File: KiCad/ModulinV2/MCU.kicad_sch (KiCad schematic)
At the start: 15 parts, among them IC1 STM32F401VET6, SW1 SW_Push, SW2 SW_Push

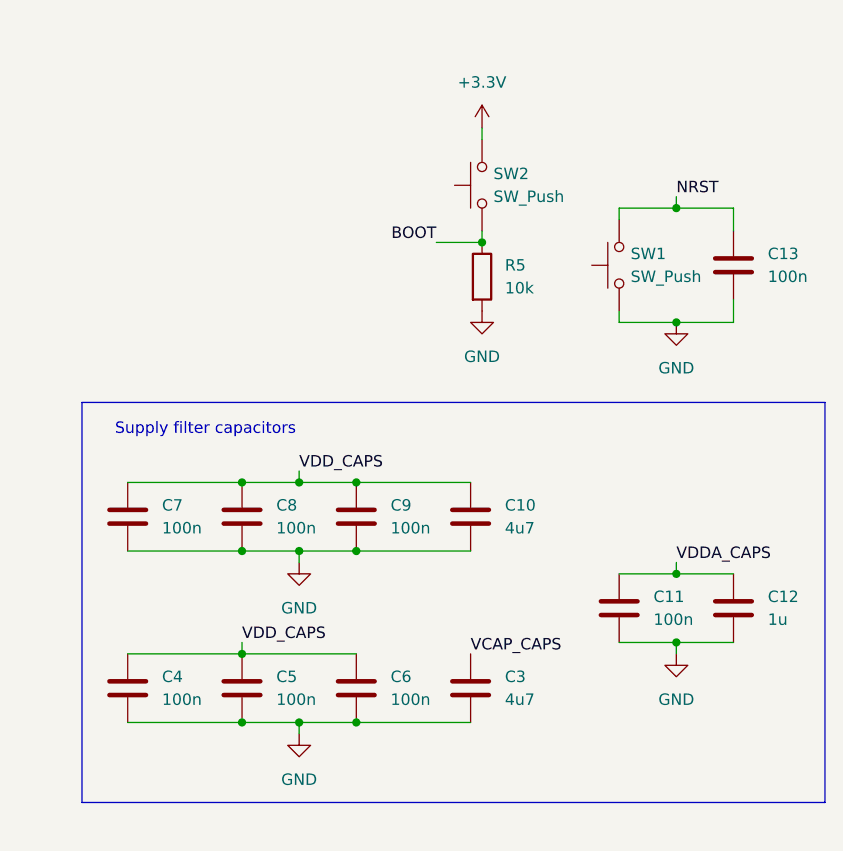
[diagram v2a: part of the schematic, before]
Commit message: Added initial schematic of VCO and repaired some schematic issues
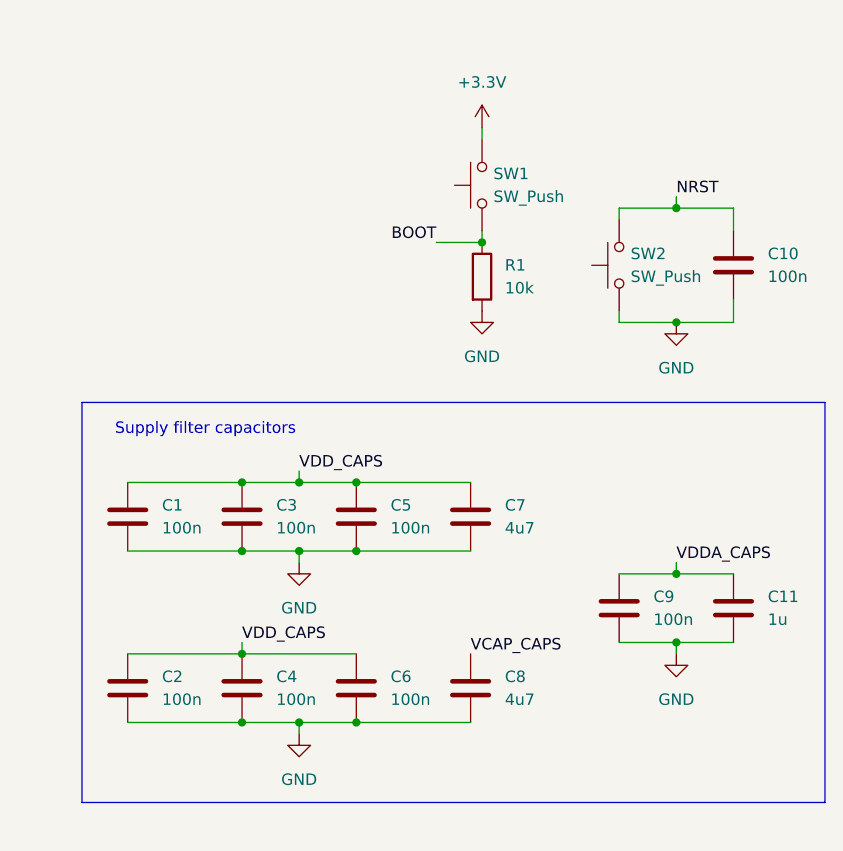
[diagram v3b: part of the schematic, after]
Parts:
- renumbered C7 to C1, C13 to C10, C12 to C11, C4 to C2, C8 to C3, C5 to C4, C9 to C5, C10 to C7, C3 to C8, C11 to C9, R5 to R1, SW2 to SW1, SW1 to SW2
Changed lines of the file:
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@@
 		(dnp no)
 		(fields_autoplaced yes)
-		(property "Reference" "C11"
+		(property "Reference" "C9"
 			(at 264.16 140.9699 0)
 			(effects
@@
 			(project "ModulinV2"
 				(path "/c6b34a57-3941-4b56-8b80-1848c7f41082/2f38494c-2f9d-4537-8bdc-28b3add05107"
-					(reference "C11")
+					(reference "C9")
 					(unit 1)
 				)
@@
 		(dnp no)
 		(fields_autoplaced yes)
-		(property "Reference" "#PWR022"
+		(property "Reference" "#PWR06"
 			(at 245.11 92.71 0)
 			(effects
@@
 			(project ""
 				(path "/c6b34a57-3941-4b56-8b80-1848c7f41082/2f38494c-2f9d-4537-8bdc-28b3add05107"
-					(reference "#PWR022")
+					(reference "#PWR06")
 					(unit 1)
 				)
@@
 		(dnp no)
 		(fields_autoplaced yes)
-		(property "Reference" "C10"
+		(property "Reference" "C7"
 			(at 247.65 130.8099 0)
 			(effects
@@
 			(project "ModulinV2"
 				(path "/c6b34a57-3941-4b56-8b80-1848c7f41082/2f38494c-2f9d-4537-8bdc-28b3add05107"
-					(reference "C10")
+					(reference "C7")
 					(unit 1)
 				)
@@
 		(dnp no)
 		(fields_autoplaced yes)
-		(property "Reference" "#PWR018"
+		(property "Reference" "#PWR09"
 			(at 266.7 153.67 0)
 			(effects
@@
 			(project "ModulinV2"
 				(path "/c6b34a57-3941-4b56-8b80-1848c7f41082/2f38494c-2f9d-4537-8bdc-28b3add05107"
-					(reference "#PWR018")
+					(reference "#PWR09")
 					(unit 1)
 				)
@@
 		(dnp no)
 		(fields_autoplaced yes)
-		(property "Reference" "#PWR020"
+		(property "Reference" "#PWR08"
 			(at 266.7 116.84 0)
 			(effects
@@
 			(project "ModulinV2"
 				(path "/c6b34a57-3941-4b56-8b80-1848c7f41082/2f38494c-2f9d-4537-8bdc-28b3add05107"
-					(reference "#PWR020")
+					(reference "#PWR08")
 					(unit 1)
 				)
@@
 		(dnp no)
 		(fields_autoplaced yes)
-		(property "Reference" "#PWR017"
+		(property "Reference" "#PWR04"
 			(at 224.79 143.51 0)
 			(effects
@@
 			(project ""
 				(path "/c6b34a57-3941-4b56-8b80-1848c7f41082/2f38494c-2f9d-4537-8bdc-28b3add05107"
-					(reference "#PWR017")
+					(reference "#PWR04")
 					(unit 1)
 				)
@@
 		(dnp no)
 		(fields_autoplaced yes)
-		(property "Reference" "#PWR019"
+		(property "Reference" "#PWR05"
 			(at 224.79 162.56 0)
 			(effects
@@
 			(project "ModulinV2"
 				(path "/c6b34a57-3941-4b56-8b80-1848c7f41082/2f38494c-2f9d-4537-8bdc-28b3add05107"
-					(reference "#PWR019")
+					(reference "#PWR05")
 					(unit 1)
 				)
@@
 		(dnp no)
 		(fields_autoplaced yes)
-		(property "Reference" "C13"
+		(property "Reference" "C10"
 			(at 276.86 102.8699 0)
 			(effects
@@
 			(project "ModulinV2"
 				(path "/c6b34a57-3941-4b56-8b80-1848c7f41082/2f38494c-2f9d-4537-8bdc-28b3add05107"
-					(reference "C13")
+					(reference "C10")
 					(unit 1)
 				)
@@
 		(dnp no)
 		(fields_autoplaced yes)
-		(property "Reference" "C12"
+		(property "Reference" "C11"
 			(at 276.86 140.9699 0)
 			(effects
@@
 			(project "ModulinV2"
 				(path "/c6b34a57-3941-4b56-8b80-1848c7f41082/2f38494c-2f9d-4537-8bdc-28b3add05107"
-					(reference "C12")
+					(reference "C11")
 					(unit 1)
 				)
@@
 		(dnp no)
 		(fields_autoplaced yes)
-		(property "Reference" "#PWR01"
+		(property "Reference" "#PWR02"
 			(at 83.82 39.37 0)
 			(effects
@@
 			(project ""
 				(path "/c6b34a57-3941-4b56-8b80-1848c7f41082/2f38494c-2f9d-4537-8bdc-28b3add05107"
-					(reference "#PWR01")
+					(reference "#PWR02")
 					(unit 1)
 				)
@@
 		(dnp no)
 		(fields_autoplaced yes)
-		(property "Reference" "R5"
+		(property "Reference" "R1"
 			(at 247.65 104.1399 0)
 			(effects
@@
 			(project ""
 				(path "/c6b34a57-3941-4b56-8b80-1848c7f41082/2f38494c-2f9d-4537-8bdc-28b3add05107"
-					(reference "R5")
+					(reference "R1")
 					(unit 1)
 				)
@@
 		(dnp no)
 		(fields_autoplaced yes)
-		(property "Reference" "SW1"
+		(property "Reference" "SW2"
 			(at 261.62 102.8699 90)
 			(effects
@@
 			(project ""
 				(path "/c6b34a57-3941-4b56-8b80-1848c7f41082/2f38494c-2f9d-4537-8bdc-28b3add05107"
-					(reference "SW1")
+					(reference "SW2")
 					(unit 1)
 				)
@@
 		(dnp no)
 		(fields_autoplaced yes)
-		(property "Reference" "C9"
+		(property "Reference" "C5"
 			(at 234.95 130.8099 0)
 			(effects
@@
 			(project "ModulinV2"
 				(path "/c6b34a57-3941-4b56-8b80-1848c7f41082/2f38494c-2f9d-4537-8bdc-28b3add05107"
-					(reference "C9")
+					(reference "C5")
 					(unit 1)
 				)
@@
 		(dnp no)
 		(fields_autoplaced yes)
-		(property "Reference" "C8"
+		(property "Reference" "C3"
 			(at 222.25 130.8099 0)
 			(effects
@@
 			(project "ModulinV2"
 				(path "/c6b34a57-3941-4b56-8b80-1848c7f41082/2f38494c-2f9d-4537-8bdc-28b3add05107"
-					(reference "C8")
+					(reference "C3")
 					(unit 1)
 				)
@@
 		(dnp no)
 		(fields_autoplaced yes)
-		(property "Reference" "SW2"
+		(property "Reference" "SW1"
 			(at 246.38 93.9799 90)
 			(effects
@@
 			(project "ModulinV2"
 				(path "/c6b34a57-3941-4b56-8b80-1848c7f41082/2f38494c-2f9d-4537-8bdc-28b3add05107"
-					(reference "SW2")
+					(reference "SW1")
 					(unit 1)
 				)
@@
 		(dnp no)
 		(fields_autoplaced yes)
-		(property "Reference" "C3"
+		(property "Reference" "C8"
 			(at 247.65 149.8599 0)
 			(effects
@@
 			(project ""
 				(path "/c6b34a57-3941-4b56-8b80-1848c7f41082/2f38494c-2f9d-4537-8bdc-28b3add05107"
-					(reference "C3")
+					(reference "C8")
 					(unit 1)
 				)
@@
 		(dnp no)
 		(fields_autoplaced yes)
-		(property "Reference" "#PWR016"
+		(property "Reference" "#PWR01"
 			(at 68.58 39.37 0)
 			(effects
@@
 			(project ""
 				(path "/c6b34a57-3941-4b56-8b80-1848c7f41082/2f38494c-2f9d-4537-8bdc-28b3add05107"
-					(reference "#PWR016")
+					(reference "#PWR01")
 					(unit 1)
 				)
@@
 		(dnp no)
 		(fields_autoplaced yes)
-		(property "Reference" "C5"
+		(property "Reference" "C4"
 			(at 222.25 149.8599 0)
 			(effects
@@
 			(project "ModulinV2"
 				(path "/c6b34a57-3941-4b56-8b80-1848c7f41082/2f38494c-2f9d-4537-8bdc-28b3add05107"
-					(reference "C5")
+					(reference "C4")
 					(unit 1)
 				)
@@
 		(dnp no)
 		(fields_autoplaced yes)
-		(property "Reference" "C7"
+		(property "Reference" "C1"
 			(at 209.55 130.8099 0)
 			(effects
@@
 			(project "ModulinV2"
 				(path "/c6b34a57-3941-4b56-8b80-1848c7f41082/2f38494c-2f9d-4537-8bdc-28b3add05107"
-					(reference "C7")
+					(reference "C1")
 					(unit 1)
 				)
@@
 		(dnp no)
 		(fields_autoplaced yes)
-		(property "Reference" "#PWR021"
+		(property "Reference" "#PWR07"
 			(at 245.11 115.57 0)
 			(effects
@@
 			(project "ModulinV2"
 				(path "/c6b34a57-3941-4b56-8b80-1848c7f41082/2f38494c-2f9d-4537-8bdc-28b3add05107"
-					(reference "#PWR021")
+					(reference "#PWR07")
 					(unit 1)
 				)
@@
 		(on_board yes)
 		(dnp no)
-		(property "Reference" "C4"
+		(property "Reference" "C2"
 			(at 209.55 149.8599 0)
 			(effects
@@
 			(project "ModulinV2"
 				(path "/c6b34a57-3941-4b56-8b80-1848c7f41082/2f38494c-2f9d-4537-8bdc-28b3add05107"
-					(reference "C4")
-					(unit 1)
-				)
+					(reference "C2")
+					(unit 1)
+				)

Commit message: Finished 1.0 of the VCO and started making the waveform select module
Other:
- company: Rasmus Palk -> (none)
- title: (none) -> Microcontroller
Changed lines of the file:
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@@
 	(paper "A4")
 	(title_block
-		(company "Rasmus Palk")
+		(title "Microcontroller")
+		(date "2025-07-13")
+		(rev "1.0")
+		(comment 1 "Instructor: Kaiser Pärnamets")
+		(comment 2 "By: Rasmus Palk")
 	)
 	(rectangle

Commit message: Modified USB connection and added LEDs
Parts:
- added C1, C13: 2u2, symbol Device:C
- added D5: CDBU0530, DIOM179X85N, symbol CDBU0530:CDBU0530
- added IC2: STM32F401RET6, symbol STM32F401RET6:STM32F401RET6_Alt
- added J1: USB4105-GF-A, symbol USB4105-GF-A:USB4105-GF-A
- added JP3, JP4: ADSR+LFO, symbol Jumper:SolderJumper_2_Open
- added LED1: 150212M173123, 150212M173123, symbol 150212M173123:150212M173123
- added LED2: 150060VS75000, LEDC1608X80N, symbol 150060VS75000:150060VS75000
- added Q3, Q4, Q5: BC847B,215, BC847B215, symbol BC847B_215:BC847B,215
- added R87, R88: 5k1, symbol Device:R
- added R89, R91: 51, symbol Device:R
- added R90: 130, symbol Device:R
- added R92, R93, R94: 68k, symbol Device:R
- added R95: 300, symbol Device:R
- C10: renamed from C7; value 4u7 -> 2u2
- C2: renamed from C8; value 4u7 -> 2u2
- renumbered C10 to C11, C2 to C12, C9 to C3, C11 to C4, C1 to C5, C4 to C6, C3 to C7, C6 to C8, C5 to C9
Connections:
- net +3.3V: now also C13.1, IC2.1 (VBAT), IC2.13 (VDDA/VREF+), IC2.19 (VDD_1), IC2.32 (VDD_2), IC2.48 (VDD_3), IC2.64 (VDD_4), LED1.1
- net BOOT: now also IC2.60 (BOOT0)
- net GND: now also C1.2, C13.2, IC2.12 (VSSA/VREF-), IC2.18 (VSS_1), IC2.31 (VSS_2), IC2.47 (VSS_3), IC2.63 (VSS_4), J1.A1 (GND), J1.A12 (GND), J1.B1 (GND), J1.B12 (GND), J1.S1 (SHIELD), LED2.1 (K), Q3.2 (E), Q4.2 (E), Q5.2 (E), R87.2, R88.2
- net NRST: now also IC2.7 (NRST)
- net ADSR_SPI_CLK renamed ADSR_CLK
- net ADSR_CLK: now also IC2.51 (PC10), JP4.1 (A)
- net ADSR_SPI_CS1 renamed ADSR_CS1
- net ADSR_CS1: now also IC2.54 (PD2)
- net ADSR_SPI_CS2 renamed ADSR_CS2
- net ADSR_CS2: now also IC2.50 (PA15)
- net ADSR_SPI_MOSI renamed ADSR_MOSI
- net ADSR_MOSI: now also IC2.53 (PC12), JP3.1 (A)
- net LFO_SPI_CLK renamed LFO_CLK
- net LFO_CLK: now also JP4.2 (B)
- net LFO_SPI_CS renamed LFO_CS
- net LFO_CS: now also IC2.40 (PC9)
- net LFO_SPI_MISO renamed LFO_MISO
- net LFO_MISO: now also IC2.52 (PC11)
- net LFO_SPI_MOSI renamed LFO_MOSI
- net LFO_MOSI: now also JP3.2 (B)
- net RIBBON_ADC_SPI_CLK renamed ADC_CLK
- net ADC_CLK: now also IC2.21 (PA5)
- net RIBBON_ADC_SPI_CS1 renamed ADC_CS1
- net ADC_CS1: now also IC2.20 (PA4)
- net RIBBON_ADC_SPI_CS2 renamed ADC_CS2
- net ADC_CS2: now also IC2.23 (PA7)
- net RIBBON_ADC_SPI_MISO renamed ADC_MISO
- net ADC_MISO: now also IC2.22 (PA6)
- net RIBBON_DAC_SPI_CLK renamed INT_DAC_CLK
- net INT_DAC_CLK: now also IC2.34 (PB13)
- net RIBBON_DAC_SPI_CS1 renamed INT_DAC_CS1
- net INT_DAC_CS1: now also IC2.33 (PB12)
- net RIBBON_DAC_SPI_CS2 renamed INT_DAC_CS2
- net INT_DAC_CS2: now also IC2.35 (PB14)
- net RIBBON_DAC_SPI_MOSI renamed INT_DAC_MOSI
- net INT_DAC_MOSI: now also IC2.36 (PB15)
- net VCAP_CAPS renamed VCAP
- net VCAP: now also C1.1, IC2.30 (VCAP1)
- new net: D5.2 (A), J1.A4 (VBUS), J1.A9 (VBUS), J1.B4 (VBUS), J1.B9 (VBUS), R95.1
- new net: LED2.2 (A), R95.2
- new net: Q3.3 (C), R89.1
- new net: LED1.2, R89.2
- new net: Q5.1 (B), R93.1
- new net: LED1.3, R91.1
- new net: LED1.4, R90.1
- new net: Q5.3 (C), R91.2
- new net: Q4.1 (B), R92.1
- new net: J1.A5 (CC1), R88.1
- new net: J1.B5 (CC2), R87.1
- new net: Q4.3 (C), R90.2
- new net: Q3.1 (B), R94.1
- new net +5V: D5.1 (K)
- new net ADSR_ENC_A: IC2.14 (PA0)
- new net ADSR_ENC_B: IC2.15 (PA1)
- new net LED_B: IC2.29 (PB10), R94.2
- new net LED_G: IC2.62 (PB9), R93.2
- new net LED_R: IC2.61 (PB8), R92.2
- new net LFO_ENC_A: IC2.41 (PA8)
- new net LFO_ENC_B: IC2.42 (PA9)
- new net SCL: IC2.58 (PB6)
- new net SDA: IC2.59 (PB7)
- new net SWCLK: IC2.49 (PA14)
- new net SWDIO: IC2.46 (PA13)
- new net SWO: IC2.55 (PB3)
- new net USB_DM: IC2.44 (PA11), J1.A7 (D-), J1.B7 (D-)
- new net USB_DP: IC2.45 (PA12), J1.A6 (D+), J1.B6 (D+)
- no-connect marks 0 -> 2
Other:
- note added: "ADSR & LFO SPI connecting"
- note added: "Reset and Boot buttons"
- note added: "VCAP"
- note added: "VDD"
- note added: "VDDA & VREF"
- note removed: "Supply filter capacitors"
- moved on the sheet: C10, C11, C12, C2, C3, C4, C5, C6, C7, C8, C9, IC1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

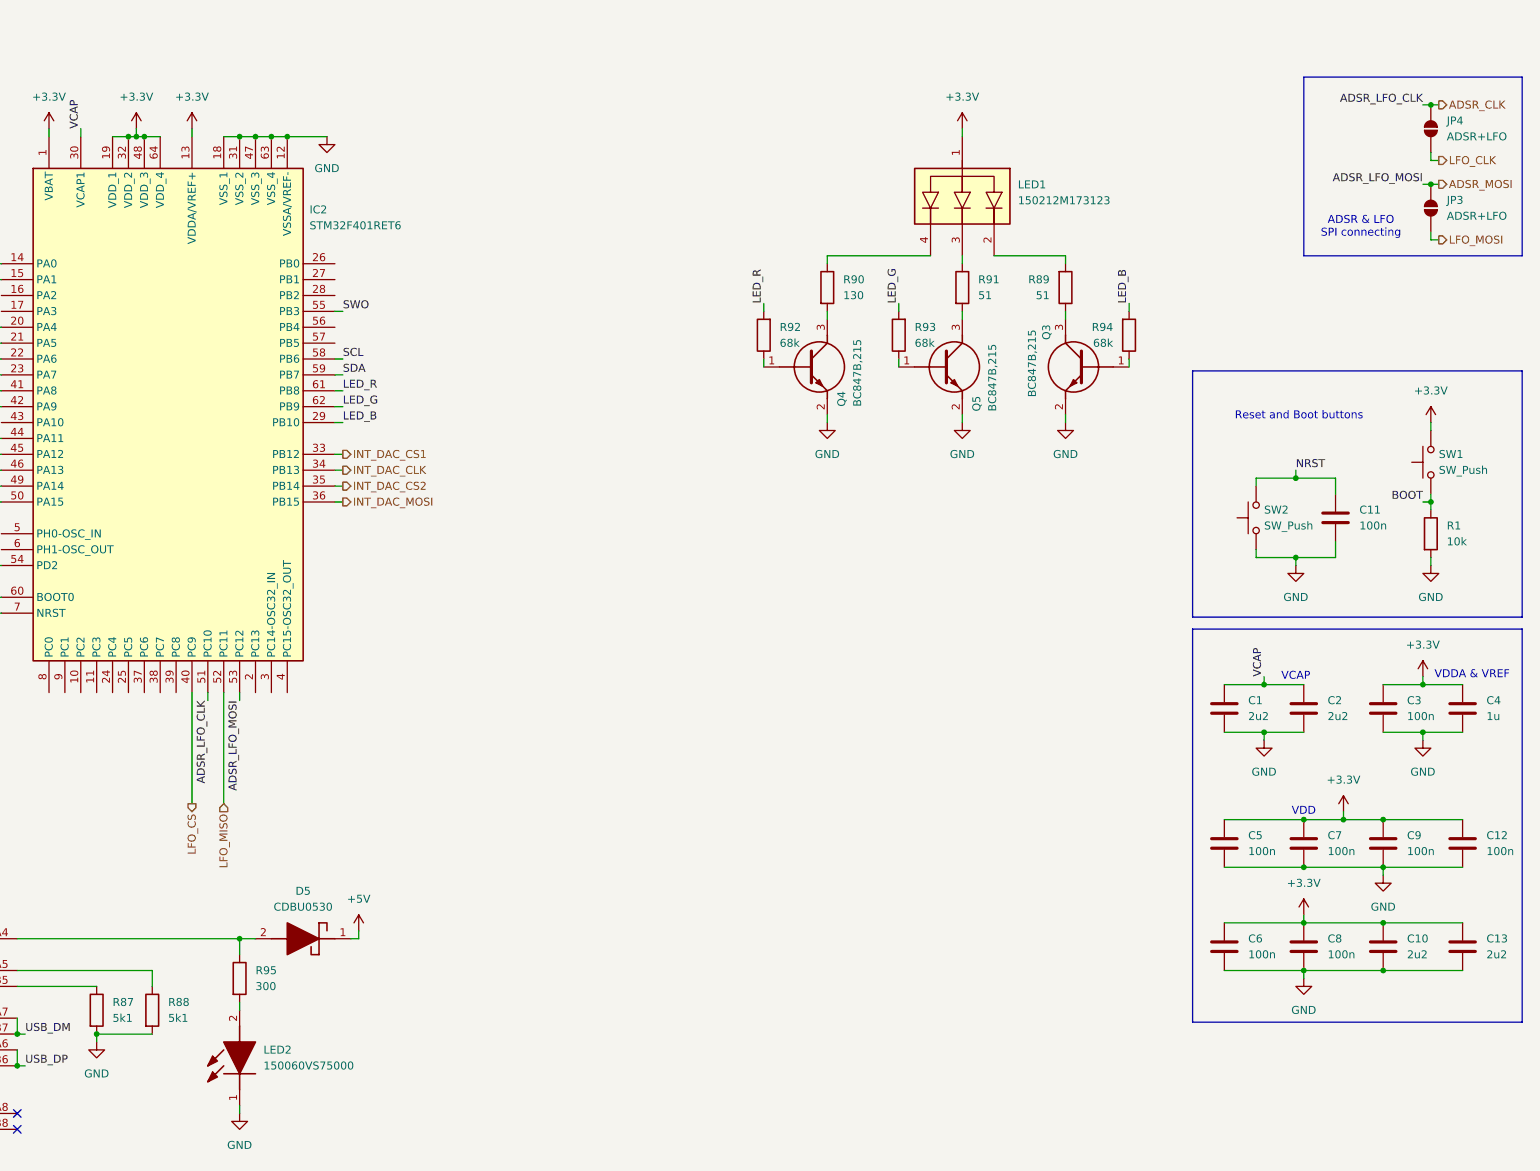
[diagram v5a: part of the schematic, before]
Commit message: Fleshed out the waveform select schematic a bit + general cleanup
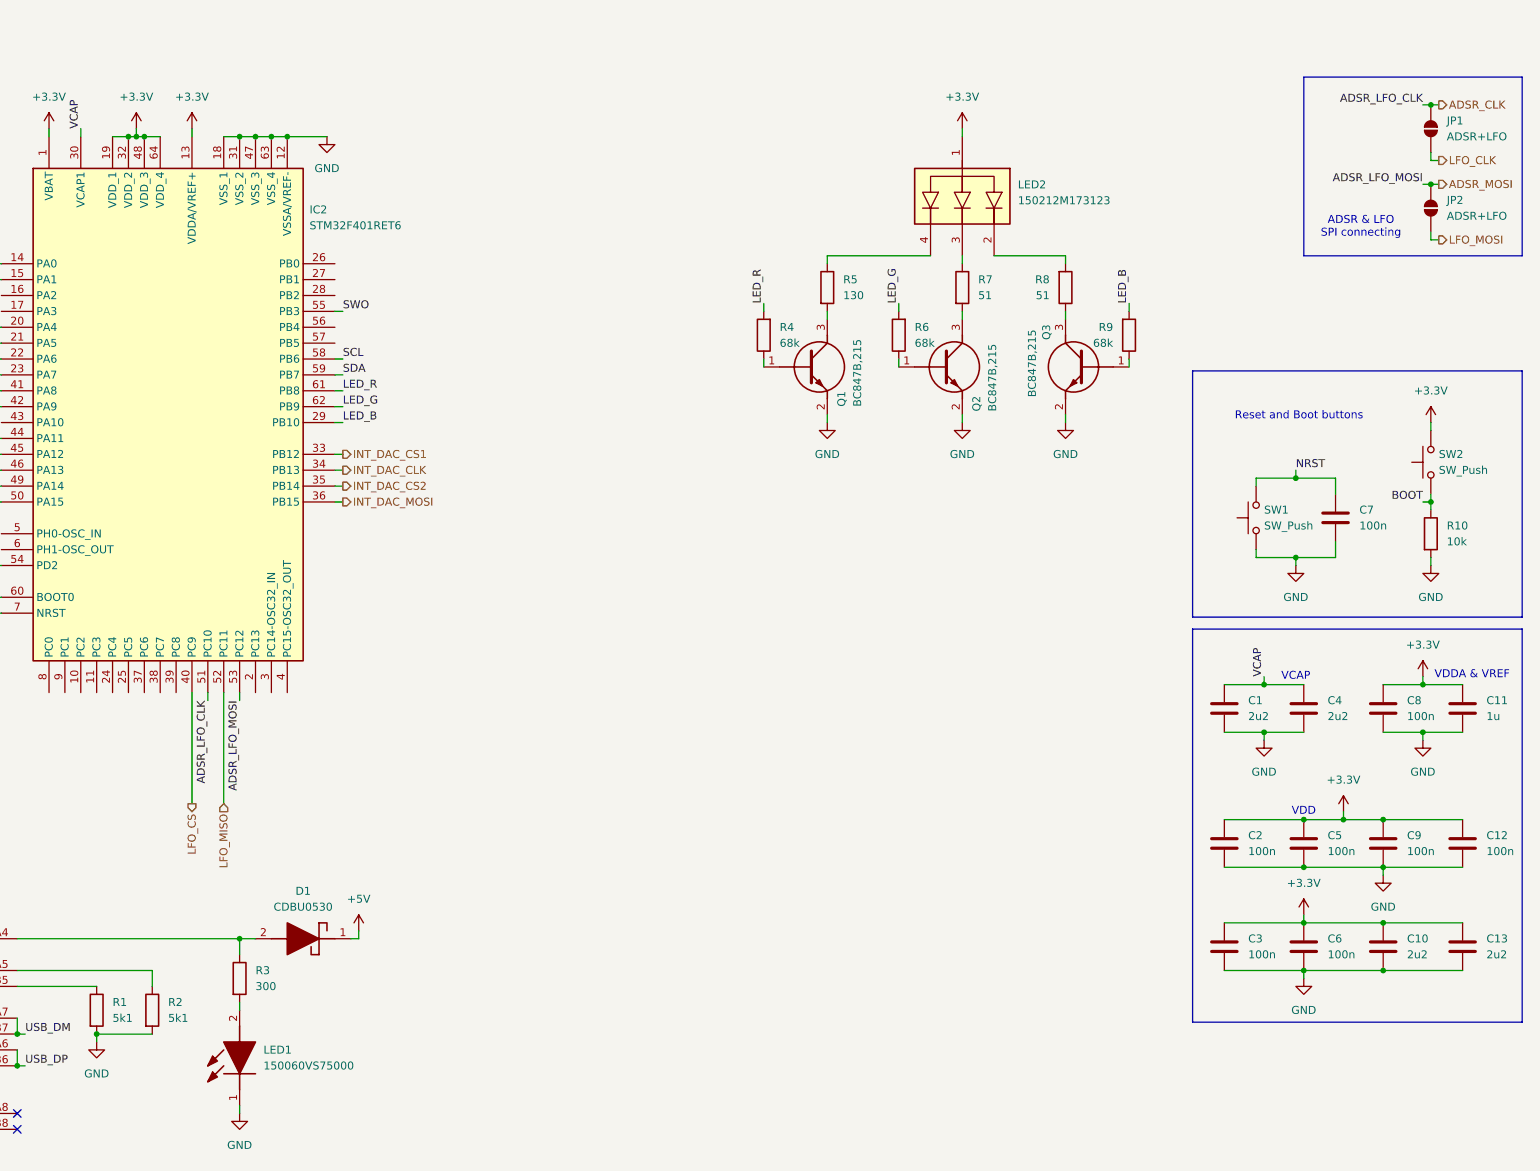
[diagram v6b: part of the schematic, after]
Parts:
- renumbered C4 to C11, C5 to C2, C6 to C3, C2 to C4, C7 to C5, C8 to C6, C11 to C7, C3 to C8, D5 to D1, JP4 to JP1, JP3 to JP2, LED2 to LED1, LED1 to LED2, Q4 to Q1, Q5 to Q2, R87 to R1, R1 to R10, R88 to R2, R95 to R3, R92 to R4, R90 to R5, R93 to R6, R91 to R7, R89 to R8, R94 to R9, SW2 to SW1, SW1 to SW2
